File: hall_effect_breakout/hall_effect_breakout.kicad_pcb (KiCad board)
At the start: 2 copper layers, 38.1 x 38.1 mm, 18 parts, among them J3 Conn_01x06, U1 AS5048A

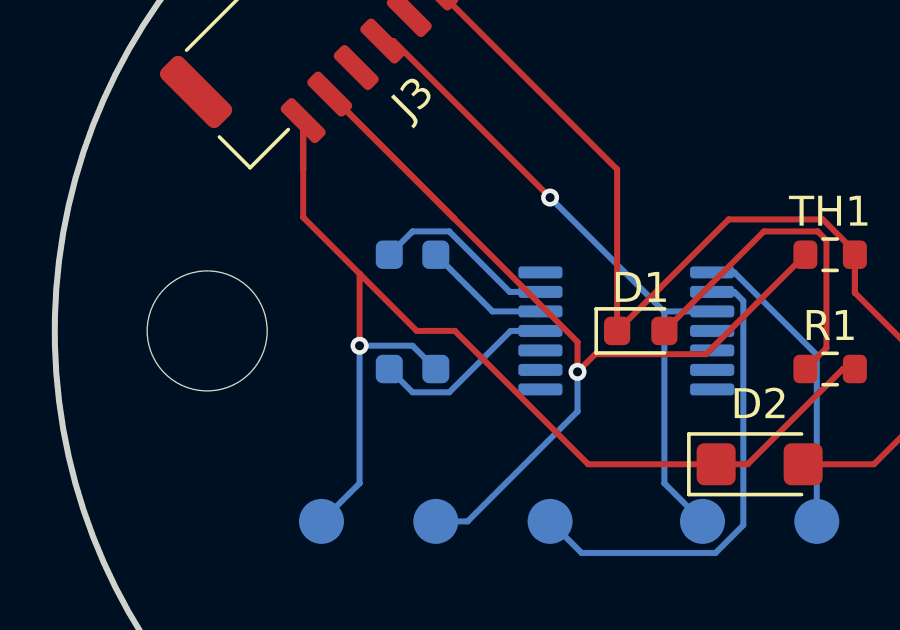
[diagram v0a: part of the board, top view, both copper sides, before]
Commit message: VDD Filtering Capacitors Changed
Changes positions of filtering capacitors to allow for easier mech integration
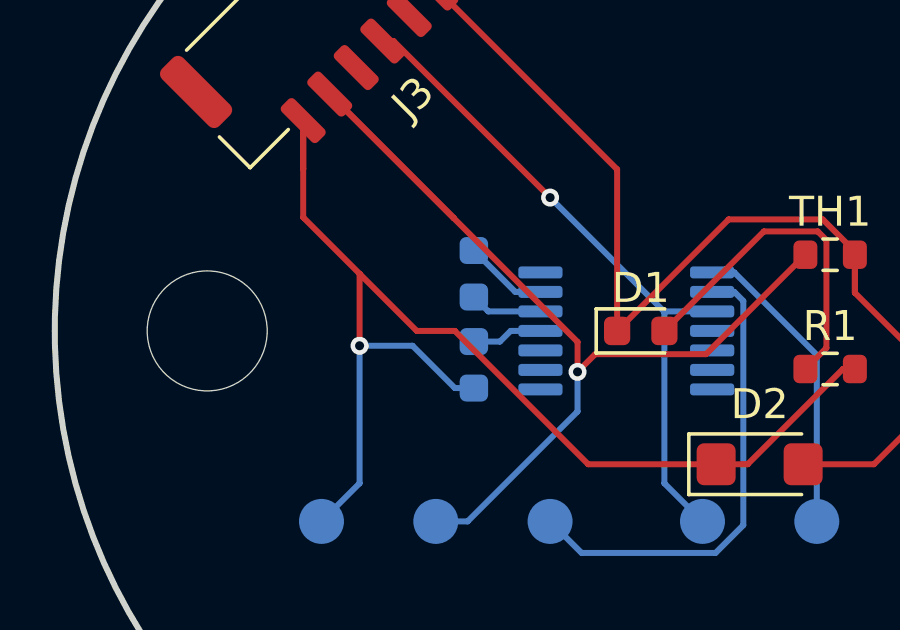
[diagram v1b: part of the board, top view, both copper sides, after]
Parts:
- moved C1 2.14 mm to (96.5, 99.7), turned to 90 degrees
- moved C2 2.05 mm to (96.5, 102.7), turned to 90 degrees
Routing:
- net Net-(U1-VDD5V): track 6.21 -> 2.36 mm
- net Net-(U1-GND): track 6.19 -> 2.79 mm
- net Net-(U1-VDD3V): track 4.27 -> 2.42 mm
- net +5V: track 39.6 -> 41.1 mm
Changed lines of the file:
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@@
 	(footprint "Capacitor_SMD:C_0603_1608Metric"
 		(layer "B.Cu")
-		(at 94.475 99.06 180)
+		(at 96.52 99.695 90)
 		(descr "Capacitor SMD 0603 (1608 Metric), square (rectangular) end terminal, IPC-7351 nominal, (Body size source: IPC-SM-782 page 76, https://www.pcb-3d.com/wordpress/wp-content/uploads/ipc-sm-782a_amendment_1_and_2.pdf), generated with kicad-footprint-generator")
 		(tags "capacitor")
 		(property "Reference" "C1"
-			(at 0 1.43 0)
+			(at 0 1.43 90)
 			(layer "B.SilkS")
 			(effects
@@
 		)
 		(property "Value" "10u"
-			(at 0 -1.43 0)
+			(at 0 -1.43 90)
 			(layer "B.Fab")
 			(effects
@@
 		)
 		(property "Datasheet" "~"
-			(at 0 0 0)
+			(at 0 0 90)
 			(layer "B.Fab")
 			(hide yes)
@@
 		)
 		(property "Description" "Unpolarized capacitor"
-			(at 0 0 0)
+			(at 0 0 90)
 			(layer "B.Fab")
 			(hide yes)
@@
 		)
 		(property "LCSC" "C90053"
-			(at 0 0 0)
+			(at 0 0 90)
 			(layer "B.SilkS")
 			(hide yes)
@@
 		(attr smd)
 		(fp_line
+			(start -0.14058 -0.51)
+			(end 0.14058 -0.51)
+			(stroke
+				(width 0.12)
+				(type solid)
+			)
+			(layer "B.SilkS")
+		)
+		(fp_line
 			(start -0.14058 0.51)
 			(end 0.14058 0.51)
@@
 		)
 		(fp_line
-			(start -0.14058 -0.51)
-			(end 0.14058 -0.51)
-			(stroke
-				(width 0.12)
-				(type solid)
-			)
-			(layer "B.SilkS")
+			(start 1.48 -0.73)
+			(end -1.48 -0.73)
+			(stroke
+				(width 0.05)
+				(type solid)
+			)
+			(layer "B.CrtYd")
+		)
+		(fp_line
+			(start -1.48 -0.73)
+			(end -1.48 0.73)
+			(stroke
+				(width 0.05)
+				(type solid)
+			)
+			(layer "B.CrtYd")
 		)
 		(fp_line
@@
 		)
 		(fp_line
-			(start 1.48 -0.73)
-			(end -1.48 -0.73)
-			(stroke
-				(width 0.05)
-				(type solid)
-			)
-			(layer "B.CrtYd")
-		)
-		(fp_line
 			(start -1.48 0.73)
 			(end 1.48 0.73)
@@
 		)
 		(fp_line
-			(start -1.48 -0.73)
-			(end -1.48 0.73)
-			(stroke
-				(width 0.05)
-				(type solid)
-			)
-			(layer "B.CrtYd")
+			(start 0.8 -0.4)
+			(end -0.8 -0.4)
+			(stroke
+				(width 0.1)
+				(type solid)
+			)
+			(layer "B.Fab")
+		)
+		(fp_line
+			(start -0.8 -0.4)
+			(end -0.8 0.4)
+			(stroke
+				(width 0.1)
+				(type solid)
+			)
+			(layer "B.Fab")
 		)
 		(fp_line
@@
 		)
 		(fp_line
-			(start 0.8 -0.4)
-			(end -0.8 -0.4)
-			(stroke
-				(width 0.1)
-				(type solid)
-			)
-			(layer "B.Fab")
-		)
-		(fp_line
 			(start -0.8 0.4)
 			(end 0.8 0.4)
@@
 			(layer "B.Fab")
 		)
-		(fp_line
-			(start -0.8 -0.4)
-			(end -0.8 0.4)
-			(stroke
-				(width 0.1)
-				(type solid)
-			)
-			(layer "B.Fab")
-		)
 		(fp_text user "${REFERENCE}"
-			(at 0 0 0)
+			(at 0 0 90)
 			(layer "B.Fab")
 			(effects
@@
 		)
 		(pad "1" smd roundrect
-			(at -0.775 0 180)
+			(at -0.775 0 90)
 			(size 0.9 0.95)
 			(layers "B.Cu" "B.Mask" "B.Paste")
@@
 		)
 		(pad "2" smd roundrect
-			(at 0.775 0 180)
+			(at 0.775 0 90)
 			(size 0.9 0.95)
 			(layers "B.Cu" "B.Mask" "B.Paste")
@@
 	(footprint "Capacitor_SMD:C_0603_1608Metric"
 		(layer "B.Cu")
-		(at 94.475 102.87 180)
+		(at 96.52 102.73 90)
 		(descr "Capacitor SMD 0603 (1608 Metric), square (rectangular) end terminal, IPC-7351 nominal, (Body size source: IPC-SM-782 page 76, https://www.pcb-3d.com/wordpress/wp-content/uploads/ipc-sm-782a_amendment_1_and_2.pdf), generated with kicad-footprint-generator")
 		(tags "capacitor")
 		(property "Reference" "C2"
-			(at 0 1.43 0)
+			(at 0 1.43 90)
 			(layer "B.SilkS")
 			(effects
@@
 		)
 		(property "Value" "100n"
-			(at 0 -1.43 0)
+			(at 0 -1.43 90)
 			(layer "B.Fab")
 			(effects
@@
 		)
 		(property "Datasheet" "~"
-			(at 0 0 0)
+			(at 0 0 90)
 			(layer "B.Fab")
 			(hide yes)
@@
 		)
 		(property "Description" "Unpolarized capacitor"
-			(at 0 0 0)
+			(at 0 0 90)
 			(layer "B.Fab")
 			(hide yes)
@@
 		)
 		(property "LCSC" "C268011"
-			(at 0 0 0)
+			(at 0 0 90)
 			(layer "B.SilkS")
 			(hide yes)
@@
 		(attr smd)
 		(fp_line
+			(start -0.14058 -0.51)
+			(end 0.14058 -0.51)
+			(stroke
+				(width 0.12)
+				(type solid)
+			)
+			(layer "B.SilkS")
+		)
+		(fp_line
 			(start -0.14058 0.51)
 			(end 0.14058 0.51)
@@
 		)
 		(fp_line
-			(start -0.14058 -0.51)
-			(end 0.14058 -0.51)
-			(stroke
-				(width 0.12)
-				(type solid)
-			)
-			(layer "B.SilkS")
+			(start 1.48 -0.73)
+			(end -1.48 -0.73)
+			(stroke
+				(width 0.05)
+				(type solid)
+			)
+			(layer "B.CrtYd")
+		)
+		(fp_line
+			(start -1.48 -0.73)
+			(end -1.48 0.73)
+			(stroke
+				(width 0.05)
+				(type solid)
+			)
+			(layer "B.CrtYd")
 		)
 		(fp_line
@@
 		)
 		(fp_line
-			(start 1.48 -0.73)
-			(end -1.48 -0.73)
-			(stroke
-				(width 0.05)
-				(type solid)
-			)
-			(layer "B.CrtYd")
-		)
-		(fp_line
 			(start -1.48 0.73)
 			(end 1.48 0.73)
@@
 		)
 		(fp_line
-			(start -1.48 -0.73)
-			(end -1.48 0.73)
-			(stroke
-				(width 0.05)
-				(type solid)
-			)
-			(layer "B.CrtYd")
+			(start 0.8 -0.4)
+			(end -0.8 -0.4)
+			(stroke
+				(width 0.1)
+				(type solid)
+			)
+			(layer "B.Fab")
+		)
+		(fp_line
+			(start -0.8 -0.4)
+			(end -0.8 0.4)
+			(stroke
+				(width 0.1)
+				(type solid)
+			)
+			(layer "B.Fab")
 		)
 		(fp_line
@@
 		)
 		(fp_line
-			(start 0.8 -0.4)
-			(end -0.8 -0.4)
-			(stroke
-				(width 0.1)
-				(type solid)
-			)
-			(layer "B.Fab")
-		)
-		(fp_line
 			(start -0.8 0.4)
 			(end 0.8 0.4)
@@
 			(layer "B.Fab")
 		)
-		(fp_line
-			(start -0.8 -0.4)
-			(end -0.8 0.4)
-			(stroke
-				(width 0.1)
-				(type solid)
-			)
-			(layer "B.Fab")
-		)
 		(fp_text user "${REFERENCE}"
-			(at 0 0 0)
+			(at 0 0 90)
 			(layer "B.Fab")
 			(effects
@@
 		)
 		(pad "1" smd roundrect
-			(at -0.775 0 180)
+			(at -0.775 0 90)
 			(size 0.9 0.95)
 			(layers "B.Cu" "B.Mask" "B.Paste")
@@
 		)
 		(pad "2" smd roundrect
-			(at 0.775 0 180)
+			(at 0.775 0 90)
 			(size 0.9 0.95)
 			(layers "B.Cu" "B.Mask" "B.Paste")
@@
 	)
 	(segment
+		(start 95.885 103.505)
+		(end 94.474 102.094)
+		(width 0.2)
+		(layer "B.Cu")
+		(net 4)
+	)
+	(segment
 		(start 92.71 106.68)
 		(end 91.44 107.95)
@@
 	)
 	(segment
-		(start 94.474 102.094)
-		(end 95.25 102.87)
-		(width 0.2)
-		(layer "B.Cu")
-		(net 4)
-	)
-	(segment
 		(start 92.71 102.094)
 		(end 92.71 106.68)
@@
 	)
 	(segment
-		(start 92.71 102.094)
-		(end 94.474 102.094)
+		(start 96.52 103.505)
+		(end 95.885 103.505)
+		(width 0.2)
+		(layer "B.Cu")
+		(net 4)
+	)
+	(segment
+		(start 94.474 102.094)
+		(end 92.71 102.094)
 		(width 0.2)
 		(layer "B.Cu")
@@
 	)
 	(segment
-		(start 94.476 103.646)
-		(end 93.7 102.87)
-		(width 0.2)
-		(layer "B.Cu")
-		(net 7)
-	)
-	(segment
-		(start 95.6991 103.646)
-		(end 94.476 103.646)
-		(width 0.2)
-		(layer "B.Cu")
-		(net 7)
-	)
-	(segment
-		(start 97.7451 101.6)
-		(end 95.6991 103.646)
-		(width 0.2)
-		(layer "B.Cu")
-		(net 7)
-	)
-	(segment
 		(start 98.7375 101.6)
 		(end 97.7451 101.6)
@@
 	)
 	(segment
-		(start 95.25 99.06)
-		(end 97.14 100.95)
+		(start 97.3901 101.955)
+		(end 97.7451 101.6)
+		(width 0.2)
+		(layer "B.Cu")
+		(net 7)
+	)
+	(segment
+		(start 96.52 101.955)
+		(end 97.3901 101.955)
+		(width 0.2)
+		(layer "B.Cu")
+		(net 7)
+	)
+	(segment
+		(start 97 100.95)
+		(end 98.7375 100.95)
 		(width 0.2)
 		(layer "B.Cu")
@@
 	)
 	(segment
-		(start 97.14 100.95)
-		(end 98.7375 100.95)
+		(start 96.52 100.47)
+		(end 97 100.95)
 		(width 0.2)
 		(layer "B.Cu")
@@
 	)
 	(segment
-		(start 97.7151 100.3)
+		(start 97.9 100.3)
 		(end 98.7375 100.3)
 		(width 0.2)
@@
 	)
 	(segment
-		(start 93.7 99.06)
-		(end 94.476 98.284)
-		(width 0.2)
-		(layer "B.Cu")
-		(net 9)
-	)
-	(segment
-		(start 95.6991 98.284)
-		(end 97.7151 100.3)
-		(width 0.2)
-		(layer "B.Cu")
-		(net 9)
-	)
-	(segment
-		(start 94.476 98.284)
-		(end 95.6991 98.284)
-		(width 0.2)
-		(layer "B.Cu")
+		(start 96.52 98.92)
+		(end 97.9 100.3)
+		(width 0.2)
+		(layer "B.Cu")

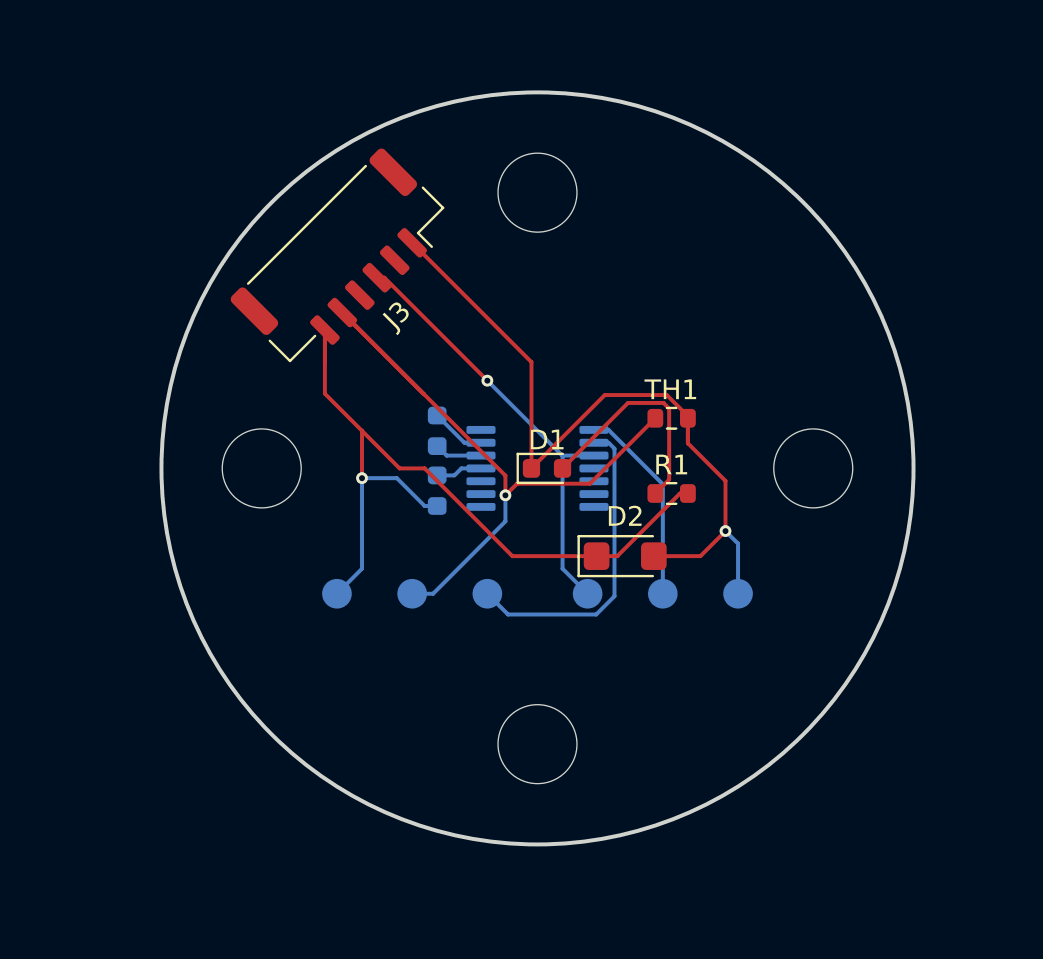
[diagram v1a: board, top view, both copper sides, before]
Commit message: Capacitor Positioning
Change capacitor position for mechanical interface
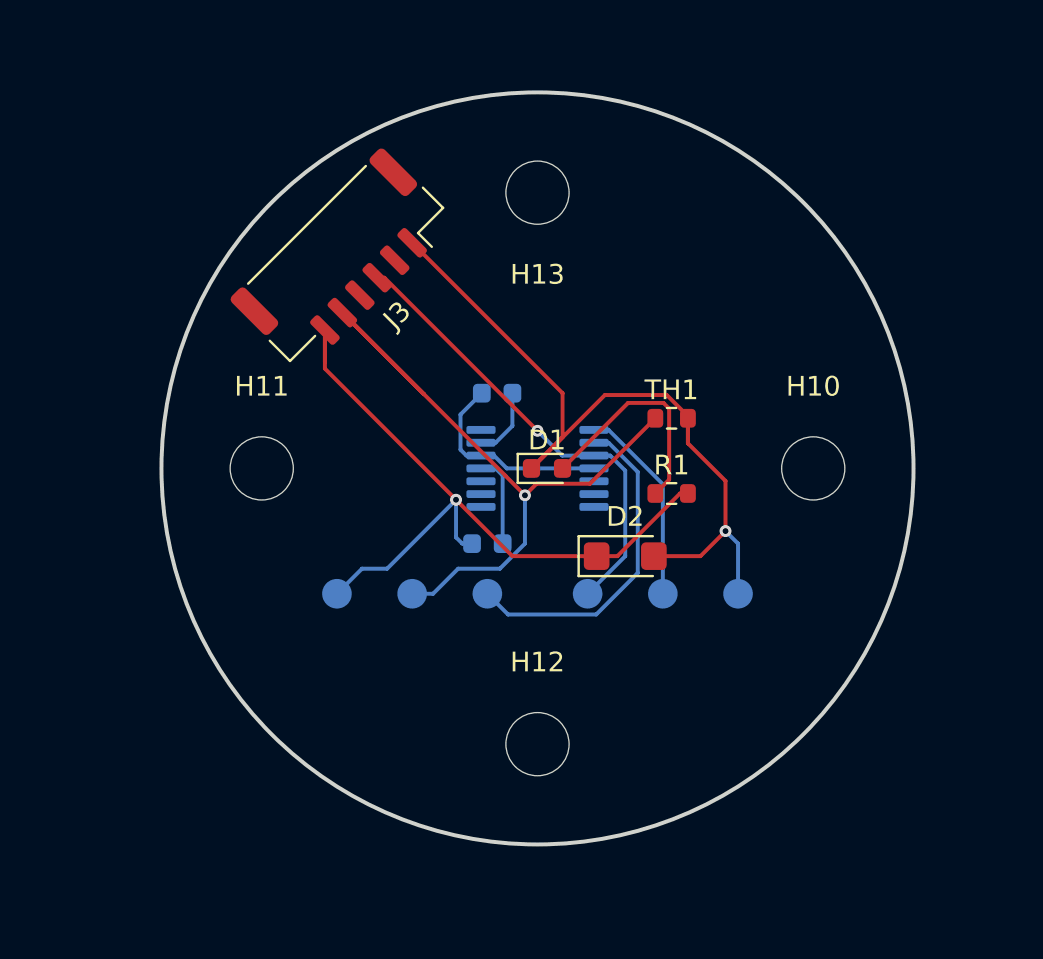
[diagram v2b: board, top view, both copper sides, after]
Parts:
- H10, H11, H12, H13: footprint MountingHole:MountingHole_4mm -> MountingHole:MountingHole_3.2mm_M3
- moved C2 3.69 mm to (99.1, 105.4), turned to 0 degrees
- moved C1 3.58 mm to (99.6, 97.8), turned to 0 degrees
- renumbered 5V to T5V, TMP to TEMP
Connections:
- C1 pad 1: Net-(U1-VDD3V) -> +3.3V
- U1 pad 12: Net-(U1-VDD3V) -> +3.3V
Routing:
- net +3.3V: track 0.00 -> 10.5 mm
- net +5V: track 41.1 -> 38.1 mm
- net Net-(U1-VDD3V): track 2.42 -> 0.00 mm
- net Net-(U1-VDD5V): track 2.36 -> 4.70 mm
- net /H2/MISO: track 22.2 -> 23.6 mm
- net GND: track 39.3 -> 40.6 mm
- net /Temp: track 35.3 -> 36.4 mm
- net /H3/SCK: track 15.9 -> 16.9 mm
- net Net-(U1-GND): track 2.79 -> 3.60 mm

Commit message: Increased trace widths and added GND filled zone
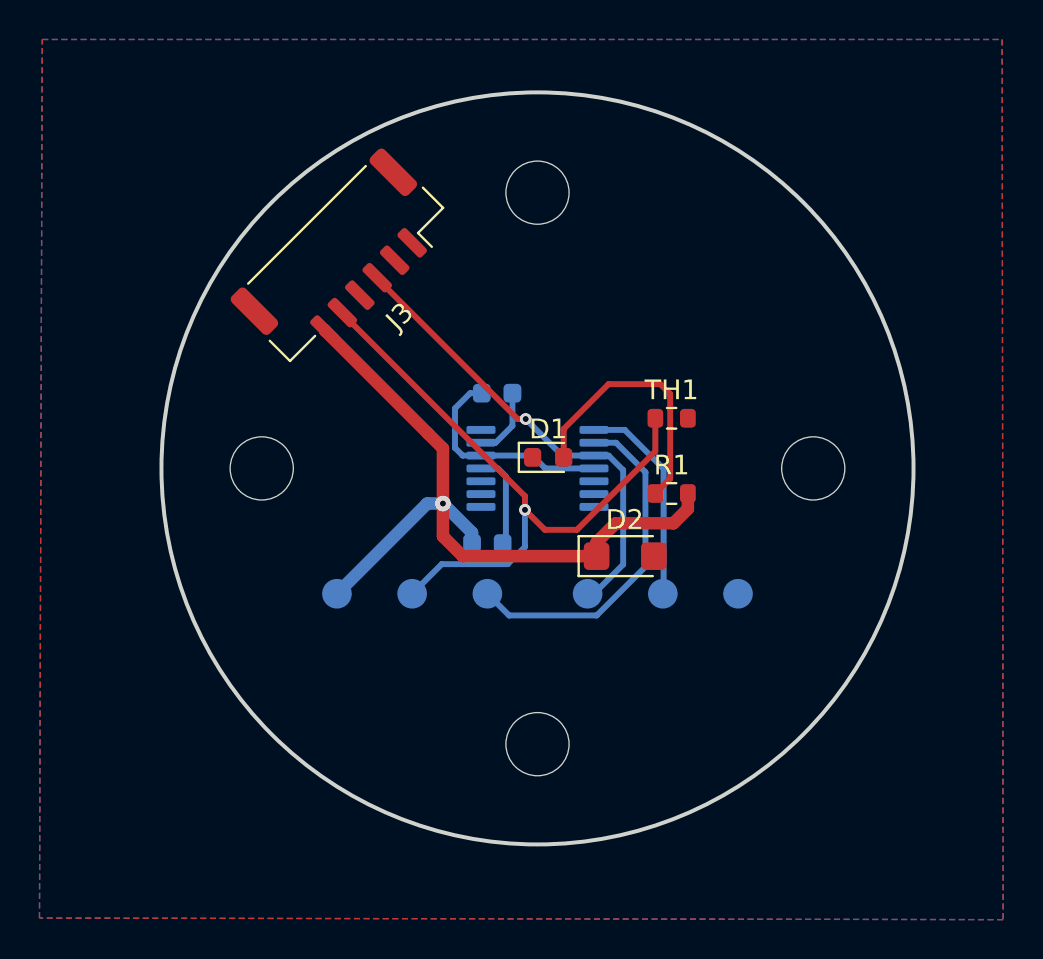
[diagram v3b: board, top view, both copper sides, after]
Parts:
- moved D1 0.56 mm to (102.1, 101.0)
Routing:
- net GND: track 40.6 -> 0.00 mm, vias 1 -> 0
- net /Temp: track 36.4 -> 32.7 mm
- net Net-(D1-A): track 11.5 -> 13.3 mm
- net +3.3V: track 10.5 -> 11.2 mm
- net /H3/SCK: track 16.9 -> 17.5 mm
- net /H1/CS: track 10.2 -> 10.7 mm
- added copper zone on B.Cu, net GND
- added copper zone on F.Cu, net GND
- added copper zone on In1.Cu, net GND
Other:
- copper layers 2 -> 4

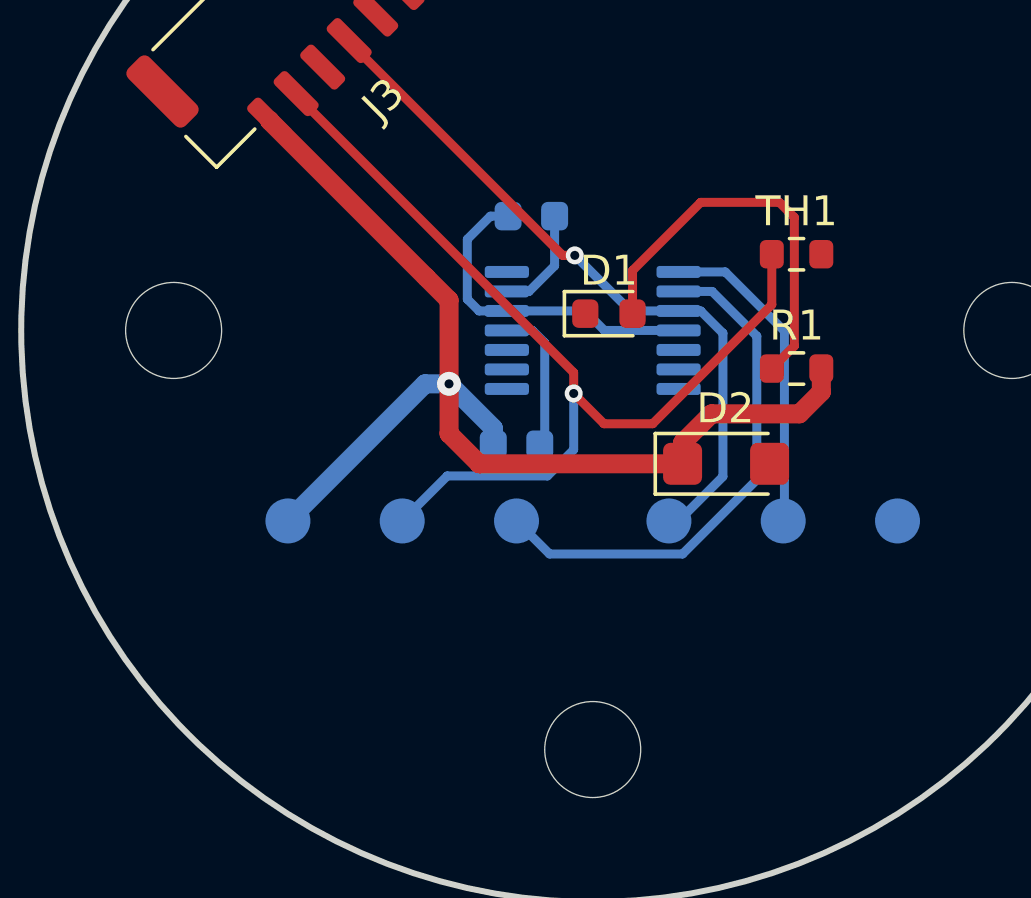
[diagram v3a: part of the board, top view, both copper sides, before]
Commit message: Silkscreen changes
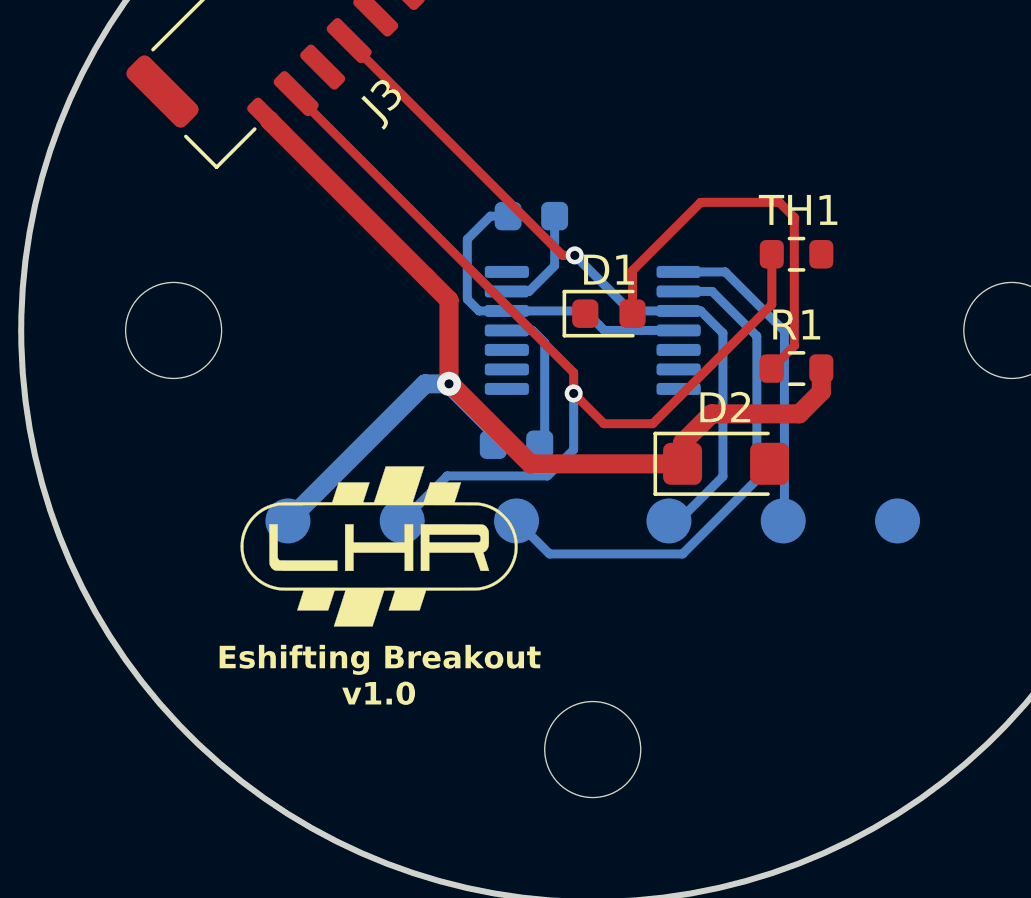
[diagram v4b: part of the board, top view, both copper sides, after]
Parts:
- added G***: LOGO, LHR:LHR_small, F.Cu at (94.5, 108.8)
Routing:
- net +5V: track 37.8 -> 36.9 mm
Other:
- board text added: "Charles Gundlach 2026"
- board text added: "Eshifting Breakout v1.0"
